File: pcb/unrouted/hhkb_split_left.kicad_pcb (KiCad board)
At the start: 2 copper layers, 138.4 x 97.4 mm, 65 parts, among them SW1 CPG151101S11-2, SW10 CPG151101S11-2, SW11 CPG151101S11-2, SW12 CPG151101S11-2, SW13 CPG151101S11-2, SW14 CPG151101S11-2, SW15 CPG151101S11-2, SW16 CPG151101S11-2, SW17 CPG151101S11-2, SW18 CPG151101S11-2, SW19 CPG151101S11-2, SW2 CPG151101S11-2, SW20 CPG151101S11-2, SW21 CPG151101S11-2, SW22 CPG151101S11-2, SW23 CPG151101S11-2, SW24 CPG151101S11-2, SW25 CPG151101S11-2, SW26 CPG151101S11-2, SW27 CPG151101S11-2, SW3 CPG151101S11-2, SW4 CPG151101S11-2, SW5 CPG151101S11-2, SW6 CPG151101S11-2, SW7 CPG151101S11-2, SW8 CPG151101S11-2, SW9 CPG151101S11-2, U1 74LVC595

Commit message: #49 利用者が左右の露出ビア（SPARE/SPARE2）を打ち直し。右の COL0 迂回と GND ビア径を当て直し、3 基板とも DRC 0
- 左右とも SPARE/SPARE2 が露出できるようになった（左 SCK は未だ）
- ⚠️ 打った場所はコネクタの奥側＝ケーブルの通り道。南側への移動を提案（open-gaps #19）

Co-Authored-By: Claude Fable 5 <noreply@anthropic.com>
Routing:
- net SPARE: track 4.03 -> 9.80 mm
- net SPARE2: track 4.48 -> 10.2 mm

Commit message: #19 決着: 右 J_DB を 1.63mm 手前へ（ソケットまで 3.9mm）、左右の配線と露出ビアを利用者が引き直し。3 基板とも DRC 0 / 未配線 0
- 右: MP パッドに当たった COL0 の迂回、V3V3 の裏面残骸 2 本を削除、MOSI ビアを 0.15mm 移動、混んだ V3V3 ビアを φ0.56（アニュラー 0.13）
- gen_pcb: 右 J_DB の dy を +1.235（中心 y=88.46）に
- 検査 458 緑・赤 1（左 SPI_SCK の露出のみ・任意）
- 記録・部品記録・DRC 記録・証拠ページを更新

Co-Authored-By: Claude Fable 5 <noreply@anthropic.com>
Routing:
- net SPARE: track 9.80 -> 14.7 mm
- net SPARE2: track 10.2 -> 13.0 mm

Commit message: #49 左の SCK・CS・V3V3 にも露出ビア（利用者）。露出は左右の全ネットがビアに。3 基板 DRC 0・検査 460 緑
Co-Authored-By: Claude Fable 5 <noreply@anthropic.com>
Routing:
- net SPI_SCK: track 18.4 -> 26.0 mm
- net CS: track 18.6 -> 25.5 mm
- net V3V3: track 31.9 -> 35.9 mm

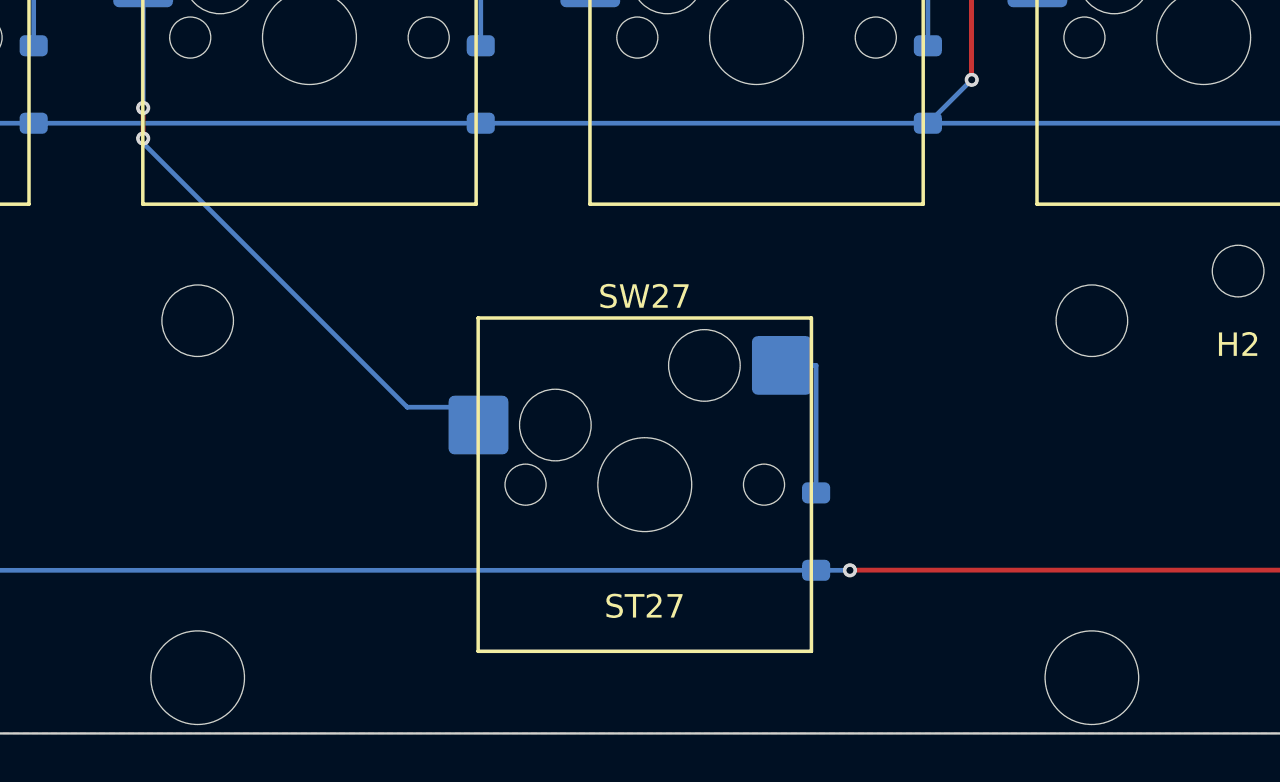
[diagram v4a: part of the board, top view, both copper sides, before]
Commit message: スペースキー 2.75u 化を基板まで反映（3 基板とも DRC 0 / 未配線 0）
設計側（29f4471）に続き、基板を作り直した。

**matrix_only のスペースキーを 2.75u へ**（KiCad の API で差し替え）:
- SW27/SW32 → SW_Hotswap_Kailh_MX_2.75u
- ST27/ST32 → Stabilizer_Cherry_MX_2.00u（穴が ±19.05 → ±11.938）
- SW/ST/D を x 左 −2.38125 / 右 +2.38125 だけ移動

**配線**: ダイオード側 2 本ずつは平行移動で端点がパッドに 0.0001mm 一致。
COL は経路の形が変わるので引き直した（左 COL3・右 COL0）。
⚠️ **利用者の指摘「col0 の配線が規則的じゃない」「col3 も」で 1 度やり直した。**
最初はクリアランスだけ見て 71.9°/2.6°/28.1°/82.9° の半端な角度で引いており、
**この板の他の配線は全部 0°/45°/90°/135°** だった。
縦→45°→水平の 3 区間に作り直し、角度を 45° の倍数に固定したまま
総当たりで障害物との距離が最大の経路を選んだ（左 +0.656mm / 右 +1.650mm）。

**シルクが 0.12mm のまま残っていたのも直した**（gen_pcb の仕上げを
通らないため。→ pcb-routing-handover.md に落とし穴として記録）。

検証: 3 基板とも 違反 0 / 未配線 0。スタビ 4 個すべて ±11.938。
STL のハウジング間隔を実測して 23.880mm（=2u）を確認。
fab_check（595 48 パッド / XIAO 14 パッド / 61 キー経路）全 OK。
基板の外形は不変（左 138.363×97.4 / 右 171.70×97.4 / 子 21.0×32.0）。
検査 464 緑。

記録: スタビの節を 2.75u 前提に書き直し、国内入手性の調査結果
（2u は潤沢・3u は買えない）と、FFC コネクタ C88360 の在庫が
40 日で 0 になるペースであることを追記。#46 の古い「次の一手」も直した。

Co-Authored-By: Claude Opus 5 (1M context) <noreply@anthropic.com>
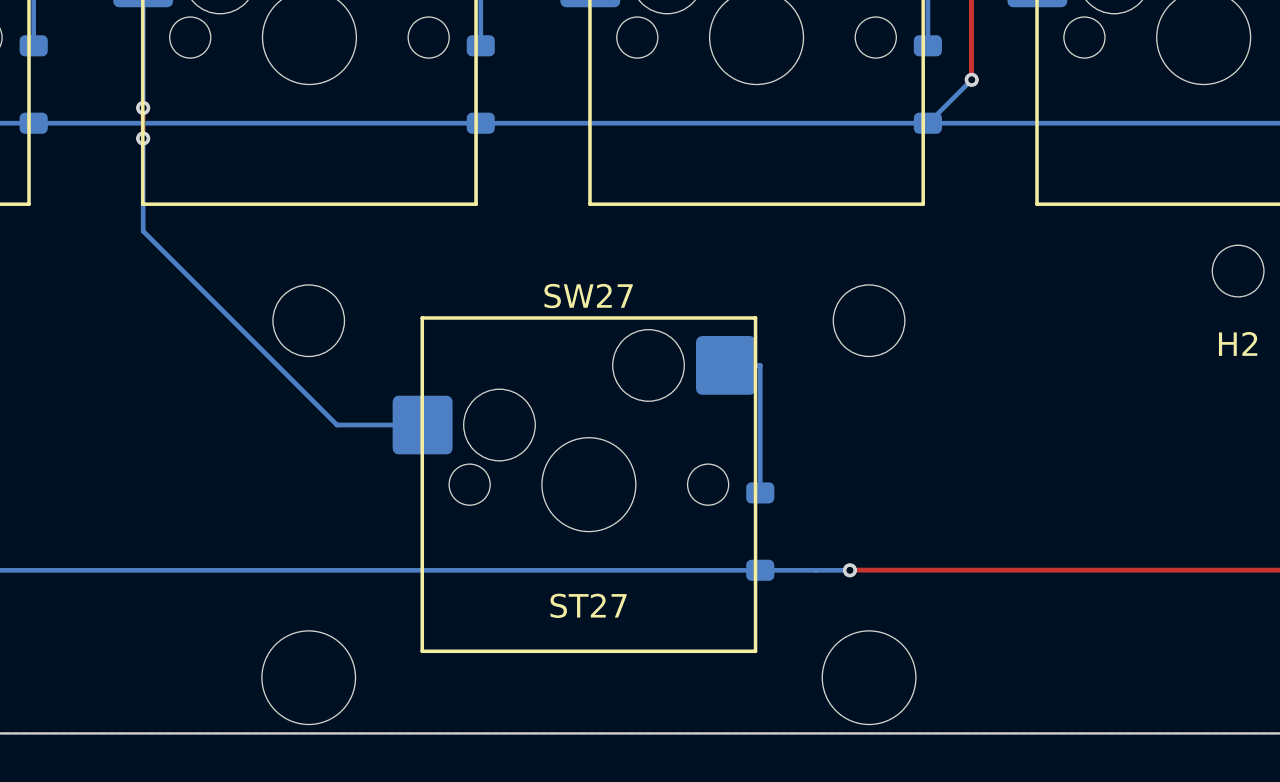
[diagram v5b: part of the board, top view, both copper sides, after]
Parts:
- ST27: value Stabilizer_Cherry_MX_3.00u -> Stabilizer_Cherry_MX_2.00u; footprint Stabilizer_Cherry_MX_3.00u -> Stabilizer_Cherry_MX_2.00u
- SW27: footprint SW_Hotswap_Kailh_MX_3.00u -> SW_Hotswap_Kailh_MX_2.75u
- moved ST27 2.38 mm to (183.3, 138.1)
- moved SW27 2.38 mm to (183.3, 138.1)
- moved D27 2.38 mm to (190.6, 140.1)
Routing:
- net COL3: track 136.0 -> 135.3 mm

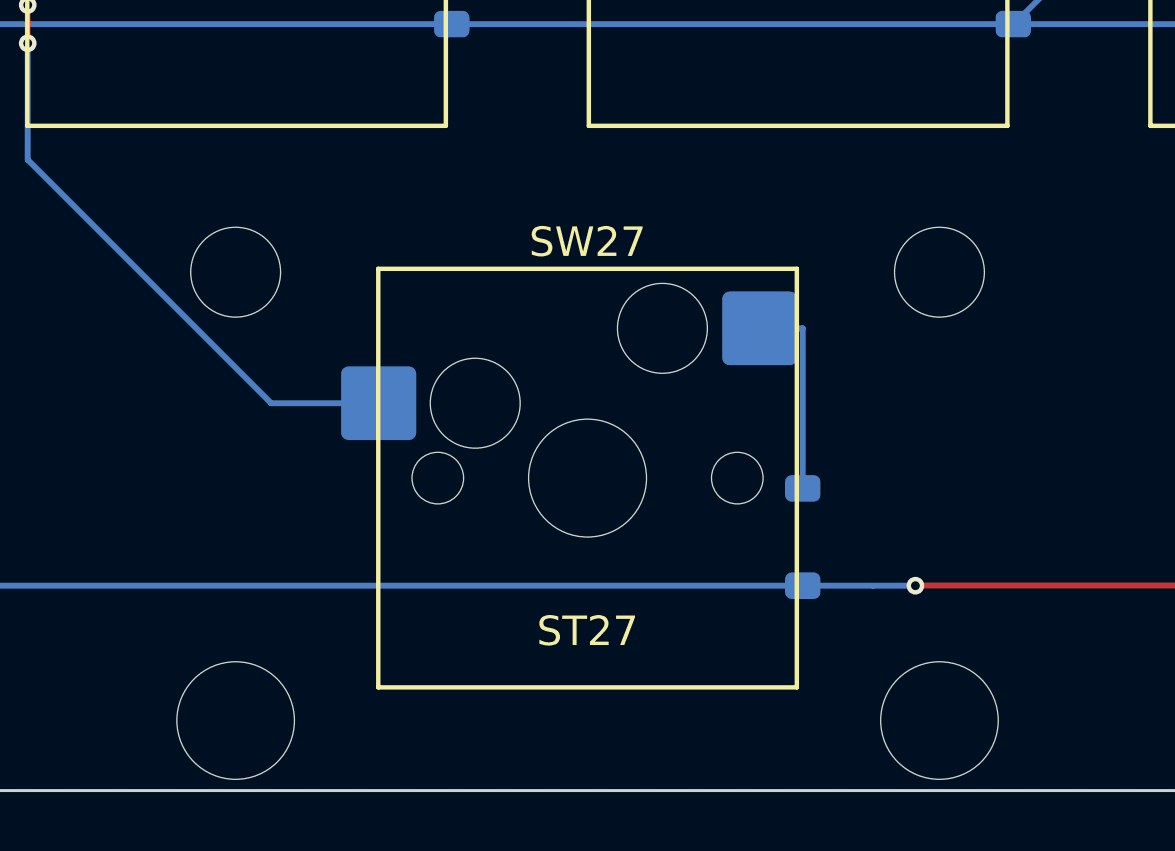
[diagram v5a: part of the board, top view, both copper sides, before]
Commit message: #53 決着: スペースのスタビ 2 個を 180°（ワイヤ奥）に回す。大穴が板前縁まで 0.381mm だったのが小穴 2.14mm に。interface.stab_flipped を gen_pcb・gen_plate・find_mounts が見る。matrix_only の ST27/ST32 を回して手順どおり再生成、3 基板 DRC 0・警告数不変。NPTH の縁 ≥1.0mm の検査を足し、回す前の板で 0.381 を検出することを確認。実形状のスタビ開口検査・test_assembly 69 件・高速 387 件緑
Co-Authored-By: Claude Fable 5 <noreply@anthropic.com>
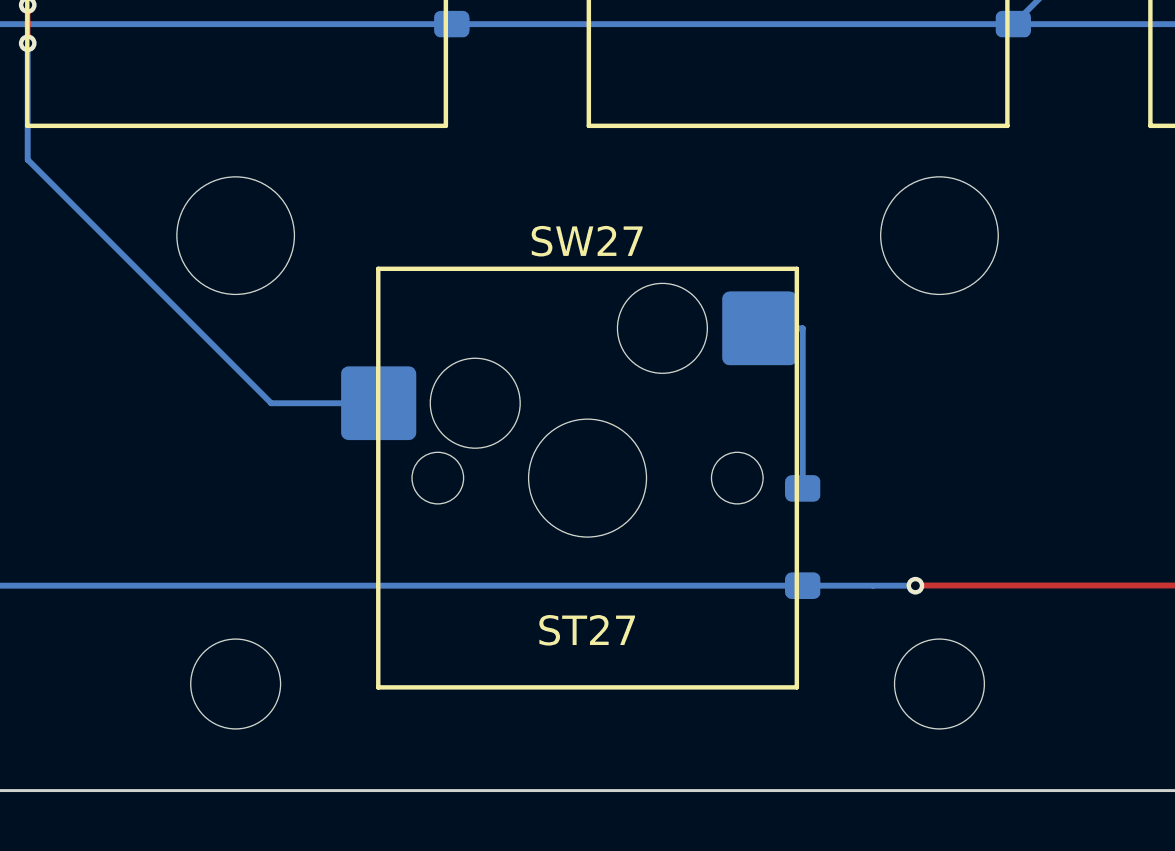
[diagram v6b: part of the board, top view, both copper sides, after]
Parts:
- turned ST27 to 180 degrees

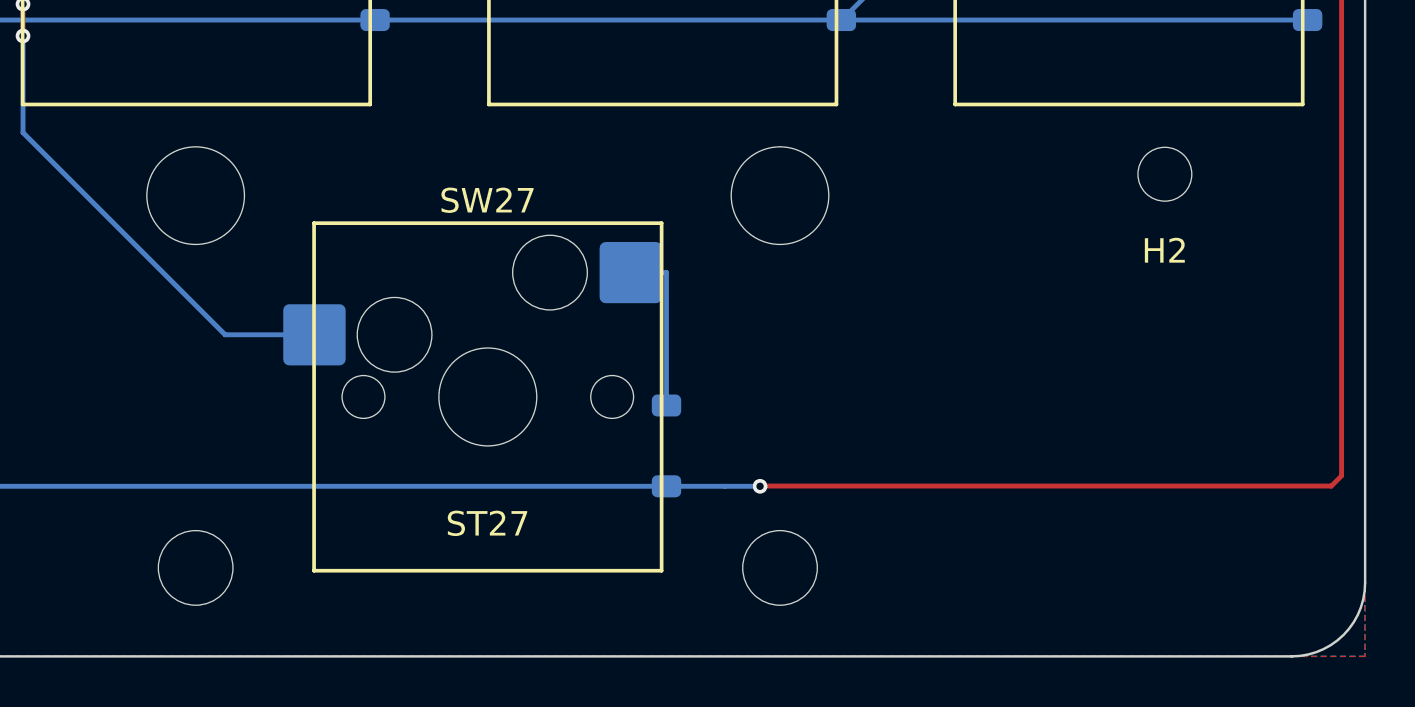
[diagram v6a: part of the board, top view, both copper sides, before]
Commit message: open-gaps #56: スペースを両島の内側端へ寄せ直し（左 4.5〜7.25u・右 9.75〜12.5u、Meta との空き左右対称 0.5u）
- layout: 最下段のみ。Alt 1u / Meta 1.5u は原機の位置のまま（利用者確認）
- 基板の柱 左 H2 (64,−30)・右 H4 (−81,−38)。柱がキーの真下に立つ取り違えを
  test_pcb_posts_do_not_touch_any_key で見る（H4 を戻すと落ちる）
- matrix_only: SW27/ST27/D27・SW32/ST32/D32 を API で移動し配線を引き直し。
  キー名シルクは部品に付いてこないので手で移動（handover の「落ちる穴」に追記）
- export_matrix_routing → gen_pcb → finalize_pcb → pcb_parts → drc。
  3 基板 DRC 0 / 未配線 0、警告は元の 37 / 41 / 1。スタビ同心 0.000・180°・縁 2.14mm
- #21: DSA 1u/1.5u/1.75u/2.25u/2.75u が SP 直販で単品・在庫ありと確認。
  2.75u の外側マウント 0.469"＝11.9mm は Cherry 2u スタビと一致
- pytest 479 passed

Co-Authored-By: Claude Fable 5 <noreply@anthropic.com>
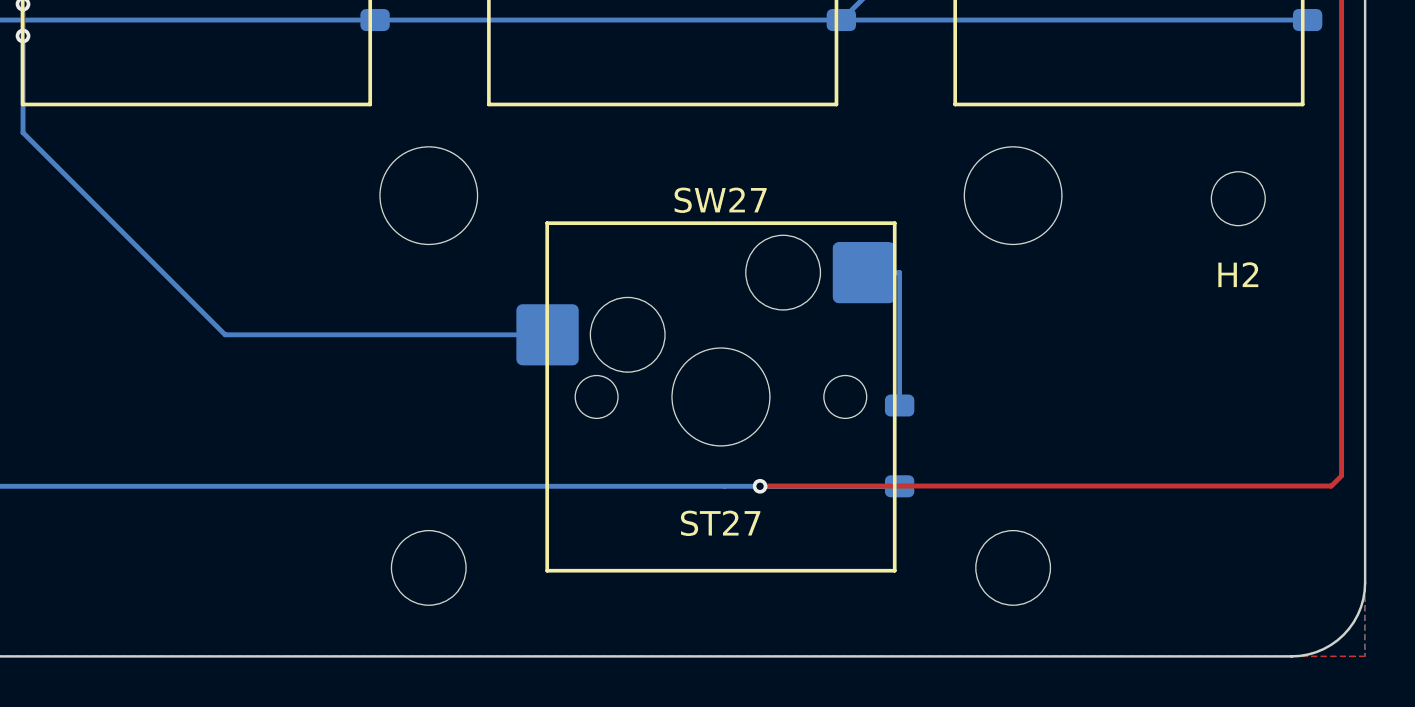
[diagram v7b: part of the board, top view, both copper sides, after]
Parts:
- moved ST27 9.53 mm to (192.9, 138.1)
- moved SW27 9.53 mm to (192.9, 138.1)
- moved D27 9.53 mm to (200.2, 140.1)
- moved H2 3.16 mm to (214.0, 130.0)
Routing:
- net COL3: track 135.3 -> 144.9 mm
- net ROW_A: track 161.7 -> 167.4 mm
